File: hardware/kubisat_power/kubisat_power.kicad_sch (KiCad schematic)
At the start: 82 parts, among them J1 USB_C_Receptacle_PowerOnly_6P, J2 B2B-PH-SM4-TB_LF__SN_, J3 Conn_01x06_MountingPin, Q1 Si2305, U2 INA3221, U3 LN2220, U4 CN3791, U5 TP4056, U6 DW01A, U7 FS8205

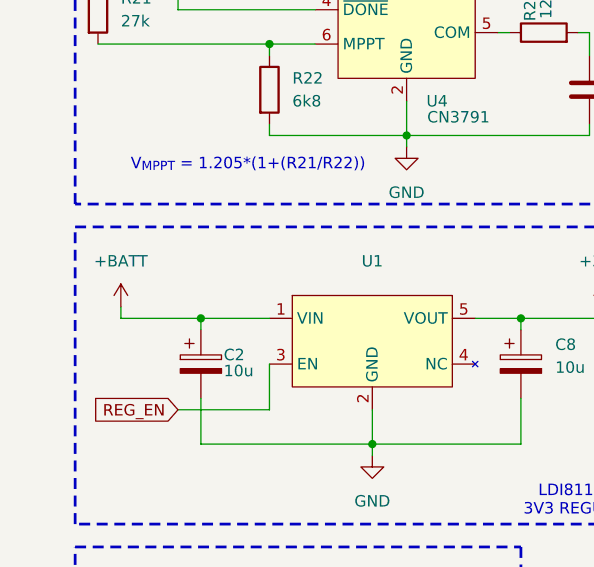
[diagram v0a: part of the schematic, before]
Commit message: added software - ina3221 and camera scripts
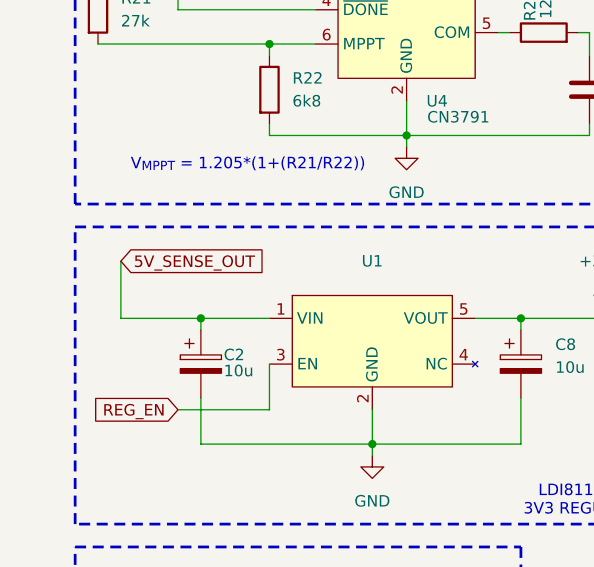
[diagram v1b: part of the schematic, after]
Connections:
- net +5V: now also C2.1, U1.1 (VIN)
- net +BATT: no longer C2.1, U1.1 (VIN)
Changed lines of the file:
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@@
 	(wire
 		(pts
+			(xy 21.59 129.54) (xy 21.59 135.89)
+		)
+		(stroke
+			(width 0)
+			(type default)
+		)
+	)
+	(wire
+		(pts
 			(xy 181.61 72.39) (xy 170.18 72.39)
 		)
@@
 	(wire
 		(pts
-			(xy 21.59 135.89) (xy 21.59 134.62)
-		)
-		(stroke
-			(width 0)
-			(type default)
-		)
-	)
-	(wire
-		(pts
 			(xy 83.82 39.37) (xy 83.82 38.1)
 		)
@@
 		)
 	)
+	(global_label "5V_SENSE_OUT"
+		(shape input)
+		(at 21.59 129.54 0)
+		(fields_autoplaced yes)
+		(effects
+			(font
+				(size 1.27 1.27)
+			)
+			(justify left)
+		)
+		(property "Intersheetrefs" "${INTERSHEET_REFS}"
+			(at 38.4846 129.54 0)
+			(effects
+				(font
+					(size 1.27 1.27)
+				)
+				(justify left)
+				(hide yes)
+			)
+		)
+	)
 	(global_label "INA3221_SCL"
 		(shape input)
@@
 					(unit 1)
 				)
-			)
-		)
-	)
-	(symbol
-		(lib_id "power:+BATT")
-		(at 21.59 134.62 0)
-		(unit 1)
-		(exclude_from_sim no)
-		(in_bom yes)
-		(on_board yes)
-		(dnp no)
-		(fields_autoplaced yes)
-		(property "Reference" "#PWR028"
-			(at 21.59 138.43 0)
-			(effects
-				(font
-					(size 1.27 1.27)
-				)
-				(hide yes)
-			)
-		)
-		(property "Value" "+BATT"
-			(at 21.59 129.54 0)
-			(effects
-				(font
-					(size 1.27 1.27)
-				)
-			)
-		)
-		(property "Footprint" ""
-			(at 21.59 134.62 0)
-			(effects
-				(font
-					(size 1.27 1.27)
-				)
-				(hide yes)
-			)
-		)
-		(property "Datasheet" ""
-			(at 21.59 134.62 0)
-			(effects
-				(font
-					(size 1.27 1.27)
-				)
-				(hide yes)
-			)
-		)
-		(property "Description" "Power symbol creates a global label with name \"+BATT\""
-			(at 21.59 134.62 0)
-			(effects
-				(font
-					(size 1.27 1.27)
-				)
-				(hide yes)
-			)
-		)
-		(pin "1"
-		)
-		(instances
-			(project ""
-				(path "/32b93b47-8cdd-4826-9733-50714c97e1cd"
-					(reference "#PWR028")
-					(unit 1)
-				)
